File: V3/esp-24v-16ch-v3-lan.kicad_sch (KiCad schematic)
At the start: 28 parts, among them J7 ETHERNET, U5 LAN8710A

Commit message: working on v3
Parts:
- removed R15, R18, R19, R20, R21, R22, R23, R25: 2k2/62,5mW/0402, Tales:R_0402_1005Metric, symbol Device:R_US
- removed R27, R28, R29, R30: 49,9R/62,5mW/0402, Tales:R_0402_1005Metric, symbol Device:R_US
- added RN1: 4x49,9R/62,5mW, Tales:R_Array_Convex_4x0402, symbol Device:R_Pack04
- added RN2, RN3: 4x2,2k/62,5mW, Tales:R_Array_Convex_4x0402, symbol Device:R_Pack04
- C14: value 1nF/2kV/1206 -> 1nF/2kV
- C15, C18, C19, C20: value 0,1uF/50V/0402 -> 0,1uF/50V
- C16, C17: value 10uF/10V/0603 -> 10uF/10V
- C21: value 1uF/25V/0402 -> 1uF/25V
- C22: value 470pF/50V/0402 -> 470pF/50V
- R16, R17: value 330R/62,5mW/0402 -> 330R/62,5mW
- R24: value 10k/62,5mW/0402 -> 10k/62,5mW; LCSC Part # C25744 -> C60490; Mfr Uniroyal -> Yageo; Mfr PN 0402WGF1002TCE -> RC0402FR-0710KL; Package (none) -> 0402/1005; Technology (none) -> 1%; Vendor PN C25744 -> C60490
- R26: value 12,1k/62,5mW/0402 -> 12,1k/62,5mW
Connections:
- net +3.3VA: now also RN1.5 (R4.2), RN1.6 (R3.2), RN1.7 (R2.2), RN1.8 (R1.2)
- net +3.3VLAN: now also R24.2, RN2.5 (R4.2), RN2.6 (R3.2), RN2.7 (R2.2), RN2.8 (R1.2), RN3.8 (R1.2); no longer R24.1
- net EMAC_MDIO: now also RN2.1 (R1.1)
- net EMAC_RX: now also RN3.1 (R1.1)
- net EMAC_RXD0: now also RN2.2 (R2.1)
- net EMAC_RXD1: now also RN2.3 (R3.1)
- net GND: now also RN3.5 (R4.2), RN3.6 (R3.2), RN3.7 (R2.2)
- net RD+: now also RN1.1 (R1.1)
- net RD-: now also RN1.2 (R2.1)
- net TD+: now also RN1.3 (R3.1)
- net TD-: now also RN1.4 (R4.1)
- net at C17.1, U5.19 (~{RST}): now also R24.1; no longer R24.2
- net at U5.13 (RXER/RXD4/~{PHYAD0}): now also RN3.2 (R2.1)
- net at U5.7 (RXCLK/~{PHYAD1}): now also RN3.4 (R4.1)
- net at U5.8 (RXD3/~{PHYAD2}): now also RN3.3 (R3.1)
- net at U5.9 (RXD2/~{RMIISEL}): now also RN2.4 (R4.1)
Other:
- moved on the sheet: C16, C18

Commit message: Added temperature sensor
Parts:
- C15, C18, C19, C20: value 0,1uF/50V -> 100nF/50V
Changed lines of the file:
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@@
 			)
 		)
-		(property "Value" "0,1uF/50V"
+		(property "Value" "100nF/50V"
 			(at 209.55 43.18 0)
 			(effects
@@
 			)
 		)
-		(property "Value" "0,1uF/50V"
+		(property "Value" "100nF/50V"
 			(at 76.2 167.6462 0)
 			(effects
@@
 			)
 		)
-		(property "Value" "0,1uF/50V"
+		(property "Value" "100nF/50V"
 			(at 153.67 38.1 0)
 			(effects
@@
 			)
 		)
-		(property "Value" "0,1uF/50V"
+		(property "Value" "100nF/50V"
 			(at 186.69 43.18 0)
 			(effects

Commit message: Renamed to V3.2
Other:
- title: ESP 16x 24VDC Input 16x 24VDC Output Module -> ESP 24V 16xIn/16xOut/4xNTC Module
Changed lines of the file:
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@@
 	(paper "A4")
 	(title_block
-		(title "ESP 16x 24VDC Input 16x 24VDC Output Module")
-		(date "2024-11-06")
-		(rev "V3")
+		(title "ESP 24V 16xIn/16xOut/4xNTC Module")
+		(date "2025-06-29")
+		(rev "V3.2")
 	)
 	(junction

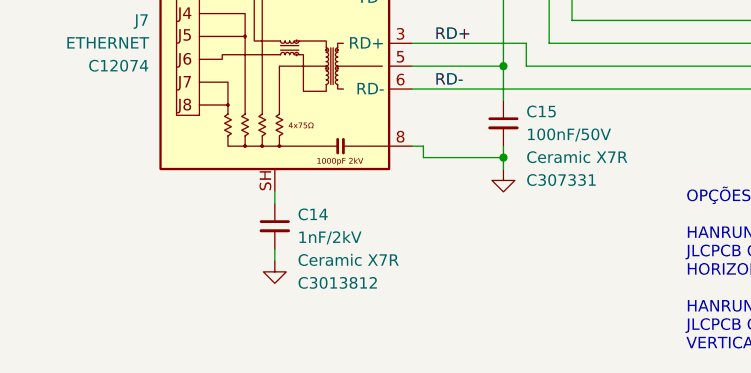
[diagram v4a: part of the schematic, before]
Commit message: Updated out of stock components
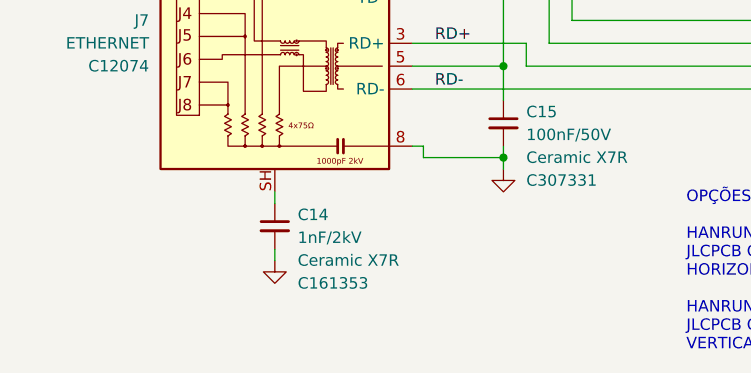
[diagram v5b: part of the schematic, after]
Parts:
- C14: LCSC Part # C3013812 -> C161353; Mfr Vishay -> Murata Electronics; Mfr PN VJ1206Y102MXFAT4X -> GR431BR7LA102KW66L; Vendor PN C3013812 -> C161353
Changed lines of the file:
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@@
 			)
 		)
-		(property "LCSC Part #" "C3013812"
+		(property "LCSC Part #" "C161353"
 			(at 50.8 184.15 0)
 			(effects
@@
 			)
 		)
-		(property "Mfr" "Vishay"
+		(property "Mfr" "Murata Electronics"
 			(at 48.26 177.8 0)
 			(effects
@@
 			)
 		)
-		(property "Mfr PN" "VJ1206Y102MXFAT4X"
+		(property "Mfr PN" "GR431BR7LA102KW66L"
 			(at 48.26 177.8 0)
 			(effects
@@
 			)
 		)
-		(property "Vendor PN" "C3013812"
+		(property "Vendor PN" "C161353"
 			(at 48.26 177.8 0)
 			(effects

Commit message: Adjusted version numbers
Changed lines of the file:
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@@
 (kicad_sch
-	(version 20231120)
+	(version 20250114)
 	(generator "eeschema")
-	(generator_version "8.0")
+	(generator_version "9.0")
 	(paper "A4")
 	(title_block
@@
 		(rev "V3.2")
 	)
+	(text "OPÇÕES RJ45\n\nHANRUN HR911105A\nJLCPCB C12074\nHORIZONTAL MAGNÉTICO\n\nHANRUN HY951180A\nJLCPCB C34677\nVERTICAL MAGNÉTICO"
+		(exclude_from_sim no)
+		(at 93.98 191.77 0)
+		(effects
+			(font
+				(size 1.27 1.27)
+			)
+			(justify left bottom)
+		)
+	)
 	(junction
 		(at 67.31 31.75)
@@
 		)
 	)
-	(text "OPÇÕES RJ45\n\nHANRUN HR911105A\nJLCPCB C12074\nHORIZONTAL MAGNÉTICO\n\nHANRUN HY951180A\nJLCPCB C34677\nVERTICAL MAGNÉTICO"
-		(exclude_from_sim no)
-		(at 93.98 191.77 0)
-		(effects
-			(font
-				(size 1.27 1.27)
-			)
-			(justify left bottom)
-		)
-	)
 	(label "RD-"
 		(at 66.04 162.56 0)
-		(fields_autoplaced yes)
 		(effects
 			(font
@@
 	(label "LED_Y_A"
 		(at 199.39 81.28 0)
-		(fields_autoplaced yes)
 		(effects
 			(font
@@
 	(label "TD+"
 		(at 66.04 147.32 0)
-		(fields_autoplaced yes)
 		(effects
 			(font
@@
 	(label "TD+"
 		(at 199.39 60.96 0)
-		(fields_autoplaced yes)
 		(effects
 			(font
@@
 	(label "TD-"
 		(at 66.04 152.4 0)
-		(fields_autoplaced yes)
 		(effects
 			(font
@@
 	(label "RD-"
 		(at 199.39 68.58 0)
-		(fields_autoplaced yes)
 		(effects
 			(font
@@
 	(label "RD+"
 		(at 66.04 157.48 0)
-		(fields_autoplaced yes)
 		(effects
 			(font
@@
 	(label "RD+"
 		(at 199.39 66.04 0)
-		(fields_autoplaced yes)
 		(effects
 			(font
@@
 	(label "LED_G_K"
 		(at 199.39 83.82 0)
-		(fields_autoplaced yes)
 		(effects
 			(font
@@
 	(label "TD-"
 		(at 199.39 63.5 0)
-		(fields_autoplaced yes)
 		(effects
 			(font
@@
 		(shape output)
 		(at 34.29 73.66 180)
-		(fields_autoplaced yes)
 		(effects
 			(font
@@
 		(shape output)
 		(at 34.29 68.58 180)
-		(fields_autoplaced yes)
 		(effects
 			(font
@@
 		(shape input)
 		(at 34.29 109.22 180)
-		(fields_autoplaced yes)
 		(effects
 			(font
@@
 		(shape input)
 		(at 34.29 78.74 180)
-		(fields_autoplaced yes)
 		(effects
 			(font
@@
 		(shape output)
 		(at 34.29 106.68 180)
-		(fields_autoplaced yes)
 		(effects
 			(font
@@
 		(shape input)
 		(at 34.29 76.2 180)
-		(fields_autoplaced yes)
 		(effects
 			(font
@@
 		(shape input)
 		(at 34.29 71.12 180)
-		(fields_autoplaced yes)
 		(effects
 			(font
@@
 		(shape output)
 		(at 34.29 58.42 180)
-		(fields_autoplaced yes)
 		(effects
 			(font
@@
 		(shape output)
 		(at 34.29 60.96 180)
-		(fields_autoplaced yes)
 		(effects
 			(font
@@
 		)
 	)
+	(embedded_fonts no)
 )
